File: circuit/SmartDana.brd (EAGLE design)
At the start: 100 x 80 mm, 18 parts

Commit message: 回転灯動作確認
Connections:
- net N$10 renamed LIGHT_LAMP
- net N$9 renamed LIGHT_MOTOR
- removed net N$11: ARDUINO_NANO1.24, LIGHT.4
- new net LIGHT_PWM: ARDUINO_NANO1.21, LIGHT.4
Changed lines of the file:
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@@
 <wire x1="-48.26" y1="49.53" x2="-38.1" y2="35.56" width="0" layer="19" extent="1-1"/>
 </signal>
-<signal name="N$9">
+<signal name="LIGHT_MOTOR">
 <contactref element="RELAY_C" pad="2"/>
 <contactref element="ARDUINO_NANO1" pad="25"/>
 <wire x1="-40.64" y1="17.78" x2="21.59" y2="50.8" width="0" layer="19" extent="1-1"/>
 </signal>
-<signal name="N$10">
+<signal name="LIGHT_LAMP">
 <contactref element="RELAY_C" pad="3"/>
 <contactref element="ARDUINO_NANO1" pad="26"/>
 <wire x1="-43.18" y1="17.78" x2="21.59" y2="53.34" width="0" layer="19" extent="1-1"/>
 </signal>
-<signal name="N$11">
+<signal name="LIGHT_PWM">
 <contactref element="LIGHT" pad="4"/>
-<contactref element="ARDUINO_NANO1" pad="24"/>
-<wire x1="-35.56" y1="35.56" x2="-38.1" y2="17.78" width="0" layer="19" extent="1-1"/>
+<contactref element="ARDUINO_NANO1" pad="21"/>
+<wire x1="-35.56" y1="35.56" x2="-30.48" y2="17.78" width="0" layer="19" extent="1-1"/>
 </signal>
 <signal name="N$12">

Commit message: NodeMCU動作テスト中
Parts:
- removed R1: (no value), rcl:0207/12
- added R9: (no value), rcl:0207/12
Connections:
- removed net N$4: ARDUINO_NANO1.29, R1.1
- new net N$1: ARDUINO_NANO1.29, R9.1
- net MISO(SDO): now also ARDUINO_NANO1.30; no longer R1.2
- net MOSI(SDI): now also R9.2; no longer ARDUINO_NANO1.30
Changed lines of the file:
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@@
 <element name="LIGHT" library="pinhead" library_urn="urn:adsk.eagle:library:325" package="1X05/90" package3d_urn="urn:adsk.eagle:package:22467/2" value="" x="-38.1" y="39.37"/>
 <element name="PS2_CON" library="pinhead" library_urn="urn:adsk.eagle:library:325" package="1X06/90" package3d_urn="urn:adsk.eagle:package:22475/2" value="" x="-21.59" y="39.37"/>
-<element name="R1" library="rcl" library_urn="urn:adsk.eagle:library:334" package="0207/12" package3d_urn="urn:adsk.eagle:package:23489/1" value="" x="-20.32" y="62.23">
-<attribute name="SPICEPREFIX" value="R" x="-20.32" y="62.23" size="1.778" layer="27" display="off"/>
-</element>
 <element name="R2" library="rcl" library_urn="urn:adsk.eagle:library:334" package="0207/12" package3d_urn="urn:adsk.eagle:package:23489/1" value="" x="-35.56" y="62.23">
 <attribute name="SPICEPREFIX" value="R" x="-35.56" y="62.23" size="1.778" layer="27" display="off"/>
@@
 <element name="R8" library="rcl" library_urn="urn:adsk.eagle:library:334" package="0207/12" package3d_urn="urn:adsk.eagle:package:23489/1" value="" x="-52.07" y="-39.37">
 <attribute name="SPICEPREFIX" value="R" x="-52.07" y="-39.37" size="1.778" layer="27" display="off"/>
+</element>
+<element name="R9" library="rcl" library_urn="urn:adsk.eagle:library:334" package="0207/12" package3d_urn="urn:adsk.eagle:package:23489/1" value="" x="-52.07" y="-53.34">
+<attribute name="SPICEPREFIX" value="R" x="-52.07" y="-53.34" size="1.778" layer="27" display="off"/>
 </element>
 </elements>
@@
 </signal>
 <signal name="MOSI(SDI)">
-<contactref element="ARDUINO_NANO1" pad="30"/>
 <contactref element="PS2_CON" pad="4"/>
 <contactref element="RFID-RC522" pad="4"/>
 <contactref element="JP1" pad="4"/>
-<wire x1="-48.26" y1="21.59" x2="-53.34" y2="17.78" width="0" layer="19" extent="1-1"/>
+<contactref element="R9" pad="2"/>
+<wire x1="-48.26" y1="21.59" x2="-45.72" y2="-53.34" width="0" layer="19" extent="1-1"/>
 <wire x1="-27.94" y1="21.59" x2="-48.26" y2="21.59" width="0" layer="19" extent="1-1"/>
 <wire x1="-20.32" y1="35.56" x2="-27.94" y2="21.59" width="0" layer="19" extent="1-1"/>
-</signal>
-<signal name="N$4">
-<contactref element="ARDUINO_NANO1" pad="29"/>
-<contactref element="R1" pad="1"/>
-<wire x1="-50.8" y1="17.78" x2="-26.67" y2="62.23" width="0" layer="19" extent="1-1"/>
 </signal>
 <signal name="N$5">
@@
 </signal>
 <signal name="MISO(SDO)">
-<contactref element="R1" pad="2"/>
 <contactref element="PS2_CON" pad="3"/>
 <contactref element="RFID-RC522" pad="3"/>
 <contactref element="JP1" pad="3"/>
-<wire x1="-22.86" y1="35.56" x2="-13.97" y2="62.23" width="0" layer="19" extent="1-1"/>
-<wire x1="-30.48" y1="21.59" x2="-22.86" y2="35.56" width="0" layer="19" extent="1-1"/>
-<wire x1="-50.8" y1="21.59" x2="-30.48" y2="21.59" width="0" layer="19" extent="1-1"/>
+<contactref element="ARDUINO_NANO1" pad="30"/>
+<wire x1="-50.8" y1="21.59" x2="-53.34" y2="17.78" width="0" layer="19" extent="1-1"/>
+<wire x1="-30.48" y1="21.59" x2="-50.8" y2="21.59" width="0" layer="19" extent="1-1"/>
+<wire x1="-22.86" y1="35.56" x2="-30.48" y2="21.59" width="0" layer="19" extent="1-1"/>
 </signal>
 <signal name="SCK">
@@
 <wire x1="-45.72" y1="2.54" x2="-58.42" y2="-11.43" width="0" layer="19" extent="1-1"/>
 </signal>
+<signal name="N$1">
+<contactref element="ARDUINO_NANO1" pad="29"/>
+<contactref element="R9" pad="1"/>
+<wire x1="-50.8" y1="17.78" x2="-58.42" y2="-53.34" width="0" layer="19" extent="1-1"/>
+</signal>
 </signals>

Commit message: パターン設計仮完了
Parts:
- removed JP1: (no value), pinhead:1X09/90
- removed LIGHT: (no value), pinhead:1X05/90
- removed RELAY: (no value), pinhead:1X06
- removed RELAY_C: (no value), pinhead:1X04/90
- added ARDUINO_POWER, SERVO_POWER: (no value), pinhead:1X02
- added JP3: (no value), pinhead:1X05
- added LCD: (no value), pinhead:1X09
- LEAD_SW: device pinhead:1X02/90 -> pinhead:1X02
- PS2_CON: device pinhead:1X06/90 -> pinhead:1X06
- R2, R3, R4, R5, R6, R7, R8, R9: device rcl:0207/12 -> rcl:0204/7
- RASPI: device pinhead:1X04/90 -> pinhead:1X04
- RC_SERVO: device pinhead:1X03/90 -> pinhead:1X03
- RFID-RC522: device pinhead:1X07/90 -> pinhead:1X07
- moved R9 135.5 mm to (33.0, 52.1), turned to 90 degrees
- moved R8 130.2 mm to (40.6, 52.1), turned to 90 degrees
- moved R7 118.9 mm to (38.1, 52.1), turned to 90 degrees
- moved R6 108.2 mm to (35.6, 52.1), turned to 90 degrees
- moved RASPI 97.9 mm to (45.7, 34.3), turned to 90 degrees
- moved RFID-RC522 90.9 mm to (33.0, 66.0)
- moved R3 79.4 mm to (27.9, 52.1), turned to 90 degrees
- moved R2 75.5 mm to (39.4, 71.1), turned to 180 degrees
- moved R5 75.2 mm to (39.4, 61.0), turned to 180 degrees
- moved ARDUINO_NANO1 67.8 mm to (33.0, 25.4), turned to 90 degrees
- moved PS2_CON 63.4 mm to (31.8, 73.7)
- moved LEAD_SW 57.8 mm to (17.8, 44.5), turned to 90 degrees
- moved R4 54.4 mm to (12.7, 24.1), turned to 270 degrees
- moved RC_SERVO 51.4 mm to (17.8, 35.6), turned to 270 degrees
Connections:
- removed net +12V: RELAY.1, RELAY.4
- removed net N$3: LIGHT.2, RELAY.2
- removed net N$8: LIGHT.3, RELAY.5
- removed net VIN: ARDUINO_NANO1.15
- new net +4.1V: RC_SERVO.2, SERVO_POWER.1
- new net VCC: ARDUINO_NANO1.15, ARDUINO_POWER.1
- net +3V3: now also LCD.1, LCD.8; no longer JP1.1, JP1.8
- net +5V: now also JP3.1; no longer RC_SERVO.2, RELAY_C.1
- net DC: now also LCD.7; no longer JP1.7
- net GND: now also ARDUINO_POWER.2, JP3.5, LCD.9, SERVO_POWER.2; no longer JP1.9, LIGHT.1, LIGHT.5, RELAY_C.4
- net LIGHT_LAMP: now also JP3.2; no longer RELAY_C.3
- net LIGHT_MOTOR: now also JP3.3; no longer RELAY_C.2
- net LIGHT_PWM: now also JP3.4; no longer LIGHT.4
- net MISO(SDO): now also LCD.3; no longer JP1.3
- net MOSI(SDI): now also LCD.4; no longer JP1.4
- net RESET2: now also LCD.6; no longer JP1.6
- net SCK: now also LCD.2; no longer JP1.2
- net SS3: now also LCD.5; no longer JP1.5
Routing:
- net GND: track 0.00 -> 349.3 mm
- net +3V3: track 0.00 -> 94.0 mm, vias 0 -> 2
- net RESET: track 0.00 -> 83.8 mm, vias 0 -> 2
- net +5V: track 0.00 -> 81.3 mm, vias 0 -> 3
- net MISO(SDO): track 0.00 -> 73.7 mm, vias 0 -> 2
- net N$6: track 0.00 -> 68.6 mm, vias 0 -> 2
- net N$7: track 0.00 -> 66.0 mm, vias 0 -> 2
- net VCC: track 0.00 -> 53.3 mm, vias 0 -> 2
- net N$5: track 0.00 -> 52.9 mm
- net N$1: track 0.00 -> 48.3 mm, vias 0 -> 2
- net N$13: track 0.00 -> 40.6 mm
- net +4.1V: track 0.00 -> 33.0 mm, vias 0 -> 2
- net N$2: track 0.00 -> 33.0 mm, vias 0 -> 2
- net N$20: track 0.00 -> 27.9 mm, vias 0 -> 1
- net N$19: track 0.00 -> 22.9 mm, vias 0 -> 2
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
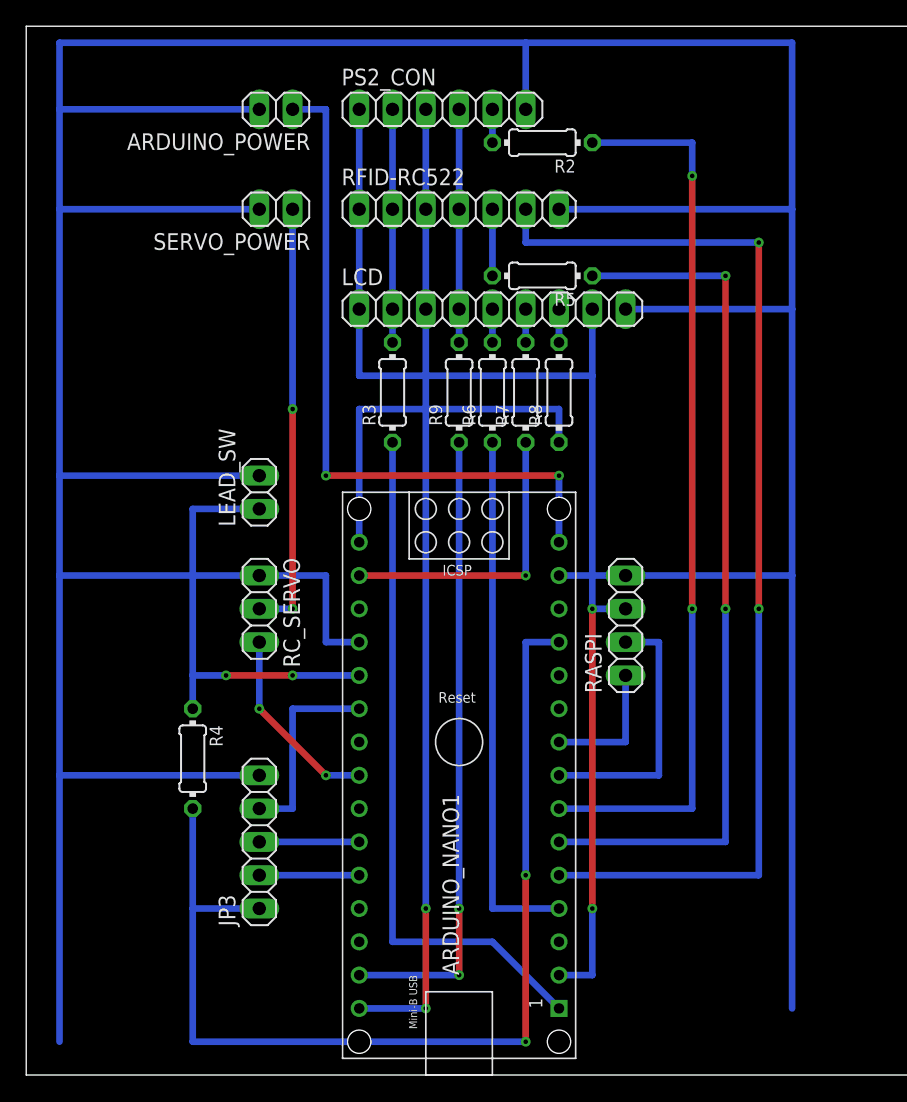
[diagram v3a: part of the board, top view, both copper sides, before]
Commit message: 体重をTCPで送信できた
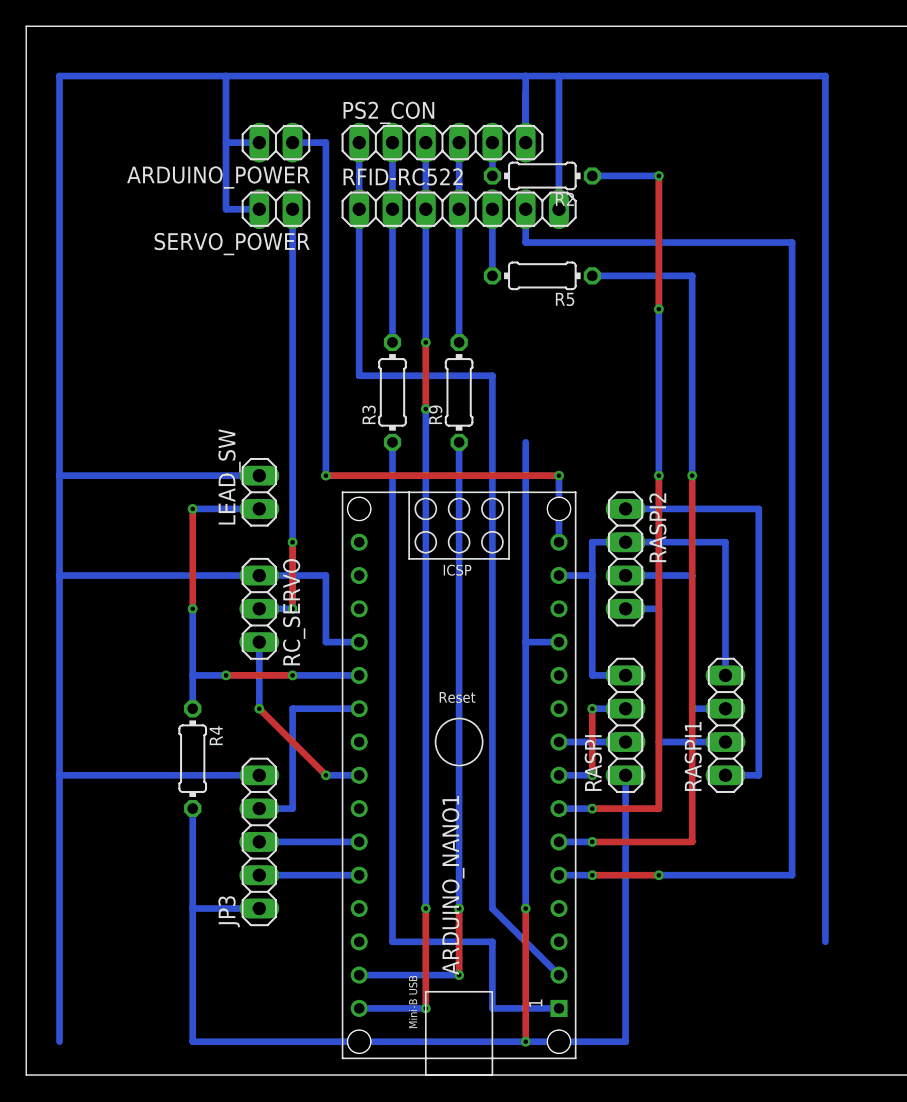
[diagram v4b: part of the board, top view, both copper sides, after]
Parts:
- removed LCD: (no value), pinhead:1X09
- removed R6, R7, R8: (no value), rcl:0204/7
- added RASPI1, RASPI2: (no value), pinhead:1X04
- moved RASPI 7.62 mm to (45.7, 26.7)
- moved R2 2.54 mm to (39.4, 68.6)
- moved ARDUINO_POWER 2.54 mm to (19.1, 71.1)
- moved PS2_CON 2.54 mm to (31.8, 71.1)
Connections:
- removed net DC: LCD.7, R8.2
- removed net N$13: ARDUINO_NANO1.4, R6.1
- removed net N$19: ARDUINO_NANO1.17, R7.1
- removed net N$20: ARDUINO_NANO1.16, R8.1
- removed net RESET2: LCD.6, R7.2
- removed net SS3: LCD.5, R6.2
- new net N$3: RASPI1.1, RASPI2.1
- new net N$8: RASPI1.2, RASPI2.4
- new net N$9: RASPI1.3, RASPI2.3
- net +3V3: no longer LCD.1, LCD.8, RASPI.3
- net +5V: now also RASPI.1
- net GND: now also RASPI1.4, RASPI2.2; no longer LCD.9
- net MISO(SDO): no longer LCD.3
- net MOSI(SDI): no longer LCD.4
- net SCK: no longer LCD.2
- net SCL: now also RASPI.2; no longer RASPI.1
- net SDA: now also RASPI.3; no longer RASPI.2
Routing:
- net +5V: track 81.3 -> 124.5 mm
- net N$13: track 40.6 -> 0.00 mm
- net N$3: track 0.00 -> 33.0 mm
- net N$20: track 27.9 -> 0.00 mm, vias 1 -> 0
- net N$19: track 22.9 -> 0.00 mm, vias 2 -> 0
- net GND: track 349.3 -> 326.4 mm
- net +3V3: track 94.0 -> 75.8 mm, vias 2 -> 0
- net N$8: track 0.00 -> 17.8 mm
- net N$9: track 0.00 -> 17.8 mm
- net SDA: track 20.3 -> 10.2 mm, vias 0 -> 2
- net N$6: track 68.6 -> 61.0 mm, vias 2 -> 4
- net N$7: track 66.0 -> 61.0 mm
- net SCL: track 10.2 -> 5.08 mm
- net RESET: track 83.8 -> 88.9 mm
- net N$5: track 52.9 -> 55.9 mm
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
